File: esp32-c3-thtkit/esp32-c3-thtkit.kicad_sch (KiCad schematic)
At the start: 27 parts, among them J1 PIN_GROUP_1, J2 PIN_GROUP_3, J3 PIN_GROUP_2, J4 UART, U1 MIC5219-3.3YM5, U2 ESP32-C3, Y1 32.768kHz ±20ppm CL12.5pF, Y2 40MHz ±10ppm CL8pF

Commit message: Change some manufacturing related attributes
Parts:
- J1, J2, TP1, TP2: now left out of the parts list
- U2: LCSC PN (none) -> C2858491
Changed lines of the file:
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@@
 		(unit 1)
 		(exclude_from_sim no)
-		(in_bom yes)
+		(in_bom no)
 		(on_board yes)
 		(dnp no)
@@
 		(unit 1)
 		(exclude_from_sim no)
-		(in_bom yes)
+		(in_bom no)
 		(on_board yes)
 		(dnp no)
@@
 		(unit 1)
 		(exclude_from_sim no)
-		(in_bom yes)
+		(in_bom no)
 		(on_board yes)
 		(dnp no)
@@
 		(unit 1)
 		(exclude_from_sim no)
-		(in_bom yes)
+		(in_bom no)
 		(on_board yes)
 		(dnp no)
@@
 			)
 		)
-		(property "LCSC PN" ""
+		(property "LCSC PN" "C2858491"
 			(at 123.19 115.57 0)
 			(effects

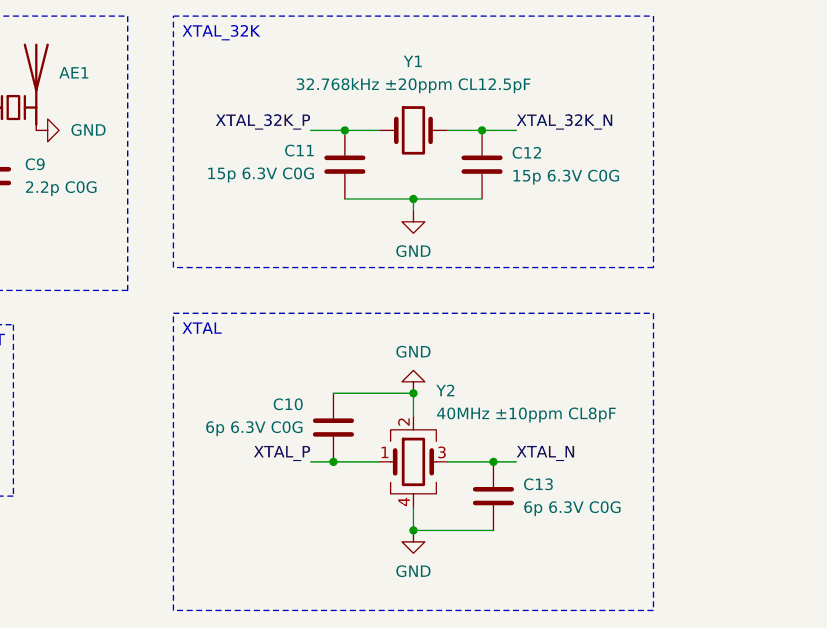
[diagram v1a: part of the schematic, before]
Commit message: Make devkits cheaper by using 0402 components instead of 0201
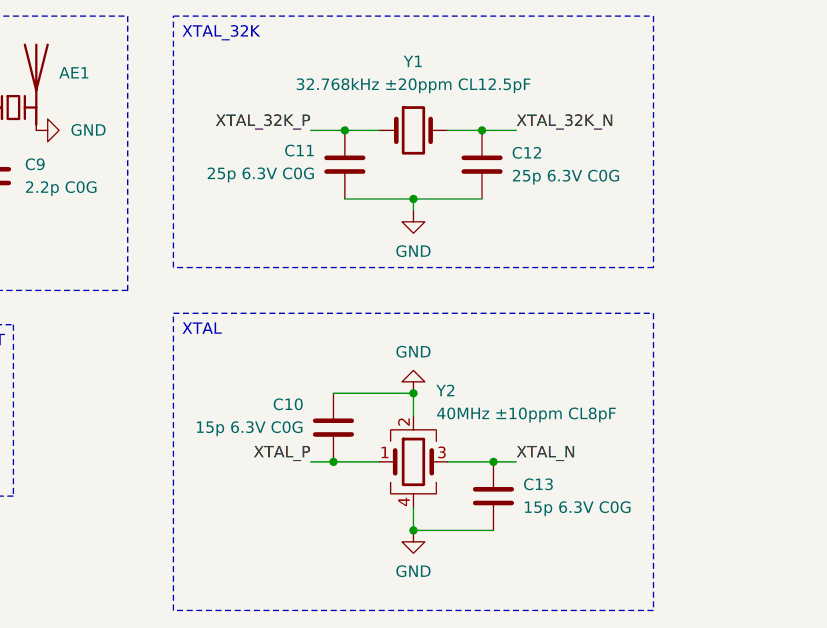
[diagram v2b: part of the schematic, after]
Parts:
- C10: value 6p 6.3V C0G -> 15p 6.3V C0G; footprint Capacitor_SMD:C_0201_0603Metric -> Capacitor_SMD:C_0402_1005Metric; LCSC PN C161434 -> C1548
- C11: value 15p 6.3V C0G -> 25p 6.3V C0G; footprint Capacitor_SMD:C_0201_0603Metric -> Capacitor_SMD:C_0402_1005Metric; LCSC PN C22374851 -> C1556
- C12: value 15p 6.3V C0G -> 25p 6.3V C0G; footprint Capacitor_SMD:C_0201_0603Metric -> Capacitor_SMD:C_0402_1005Metric; LCSC PN C237455 -> C1556
- C13: value 6p 6.3V C0G -> 15p 6.3V C0G; footprint Capacitor_SMD:C_0201_0603Metric -> Capacitor_SMD:C_0402_1005Metric; LCSC PN C237455 -> C1548
- C2: footprint Capacitor_SMD:C_0201_0603Metric -> Capacitor_SMD:C_0402_1005Metric; LCSC PN C694489 -> C1537
- C7: footprint Capacitor_SMD:C_0201_0603Metric -> Capacitor_SMD:C_0402_1005Metric; LCSC PN C85914 -> C1574
- C9: footprint Capacitor_SMD:C_0201_0603Metric -> Capacitor_SMD:C_0402_1005Metric; LCSC PN C710732 -> C1559
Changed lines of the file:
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@@
 		(title "ESP32-C3-THTKIT")
 		(date "2025-05-31")
-		(rev "1.0.0")
+		(rev "1.0.1")
 		(company "SIVAKOV.TECH")
 	)
@@
 			)
 		)
-		(property "Value" "6p 6.3V C0G"
+		(property "Value" "15p 6.3V C0G"
 			(at 212.598 132.08 0)
 			(effects
@@
 			)
 		)
-		(property "Footprint" "Capacitor_SMD:C_0201_0603Metric"
+		(property "Footprint" "Capacitor_SMD:C_0402_1005Metric"
 			(at 214.9348 128.27 0)
 			(effects
@@
 			)
 		)
-		(property "LCSC PN" "C161434"
+		(property "LCSC PN" "C1548"
 			(at 215.9 132.08 0)
 			(effects
@@
 			)
 		)
-		(property "Footprint" "Capacitor_SMD:C_0201_0603Metric"
+		(property "Footprint" "Capacitor_SMD:C_0402_1005Metric"
 			(at 176.8348 100.33 0)
 			(effects
@@
 			)
 		)
-		(property "LCSC PN" "C710732"
+		(property "LCSC PN" "C1559"
 			(at 177.8 104.14 0)
 			(effects
@@
 			)
 		)
-		(property "Footprint" "Capacitor_SMD:C_0201_0603Metric"
+		(property "Footprint" "Capacitor_SMD:C_0402_1005Metric"
 			(at 79.0448 58.42 0)
 			(effects
@@
 			)
 		)
-		(property "LCSC PN" "C694489"
+		(property "LCSC PN" "C1537"
 			(at 80.01 62.23 0)
 			(effects
@@
 			)
 		)
-		(property "Footprint" "Capacitor_SMD:C_0201_0603Metric"
+		(property "Footprint" "Capacitor_SMD:C_0402_1005Metric"
 			(at 167.64 100.0252 0)
 			(effects
@@
 			)
 		)
-		(property "LCSC PN" "C85914"
+		(property "LCSC PN" "C1574"
 			(at 171.45 99.06 90)
 			(effects
@@
 			)
 		)
-		(property "Value" "6p 6.3V C0G"
+		(property "Value" "15p 6.3V C0G"
 			(at 236.982 140.97 0)
 			(effects
@@
 			)
 		)
-		(property "Footprint" "Capacitor_SMD:C_0201_0603Metric"
+		(property "Footprint" "Capacitor_SMD:C_0402_1005Metric"
 			(at 232.7148 135.89 0)
 			(effects
@@
 			)
 		)
-		(property "LCSC PN" "C237455"
+		(property "LCSC PN" "C1548"
 			(at 233.68 139.7 0)
 			(effects
@@
 			)
 		)
-		(property "Value" "15p 6.3V C0G"
+		(property "Value" "25p 6.3V C0G"
 			(at 213.868 103.886 0)
 			(effects
@@
 			)
 		)
-		(property "Footprint" "Capacitor_SMD:C_0201_0603Metric"
+		(property "Footprint" "Capacitor_SMD:C_0402_1005Metric"
 			(at 216.2048 99.06 0)
 			(effects
@@
 			)
 		)
-		(property "LCSC PN" "C22374851"
+		(property "LCSC PN" "C1556"
 			(at 217.17 102.87 0)
 			(effects
@@
 			)
 		)
-		(property "Value" "15p 6.3V C0G"
+		(property "Value" "25p 6.3V C0G"
 			(at 235.712 104.14 0)
 			(effects
@@
 			)
 		)
-		(property "Footprint" "Capacitor_SMD:C_0201_0603Metric"
+		(property "Footprint" "Capacitor_SMD:C_0402_1005Metric"
 			(at 231.4448 99.06 0)
 			(effects
@@
 			)
 		)
-		(property "LCSC PN" "C237455"
+		(property "LCSC PN" "C1556"
 			(at 232.41 102.87 0)
 			(effects

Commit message: Change microcontroller package from 4x4 to 5x5
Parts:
- U2: footprint PCM_SKC_MCU_Espressif:TQFN_32_1EP_4x4mm_P0.4mm_EP2.4x2.4mm_Compact -> PCM_SKC_MCU_Espressif:VFQFN_32_1EP_5x5mm_P0.5mm_EP3.2x3.2mm_Compact
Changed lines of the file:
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@@
 			)
 		)
-		(property "Footprint" "PCM_SKC_MCU_Espressif:TQFN_32_1EP_4x4mm_P0.4mm_EP2.4x2.4mm_Compact"
+		(property "Footprint" "PCM_SKC_MCU_Espressif:VFQFN_32_1EP_5x5mm_P0.5mm_EP3.2x3.2mm_Compact"
 			(at 97.79 85.09 0)
 			(effects

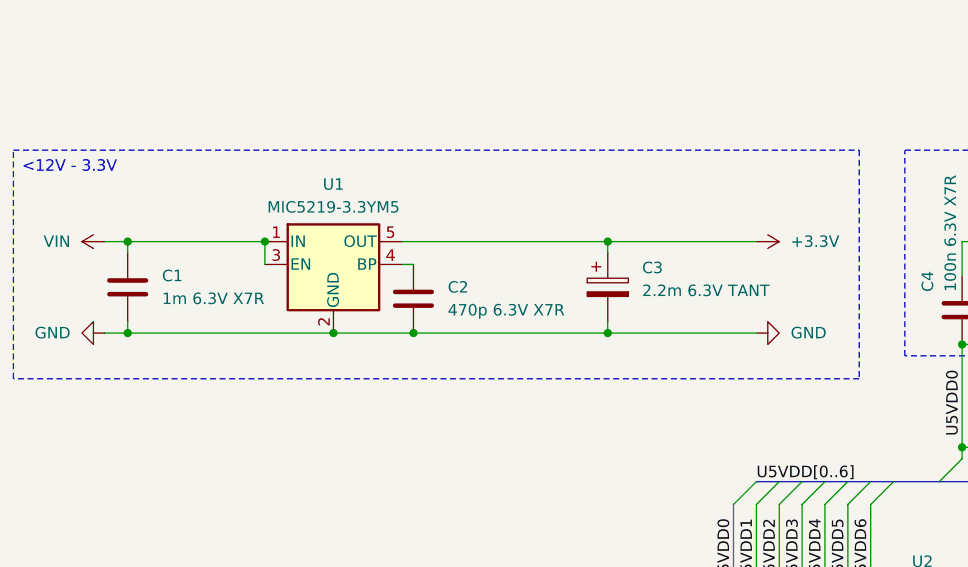
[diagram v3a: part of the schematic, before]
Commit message: Unify schemas and fix esp32-c3 footprint
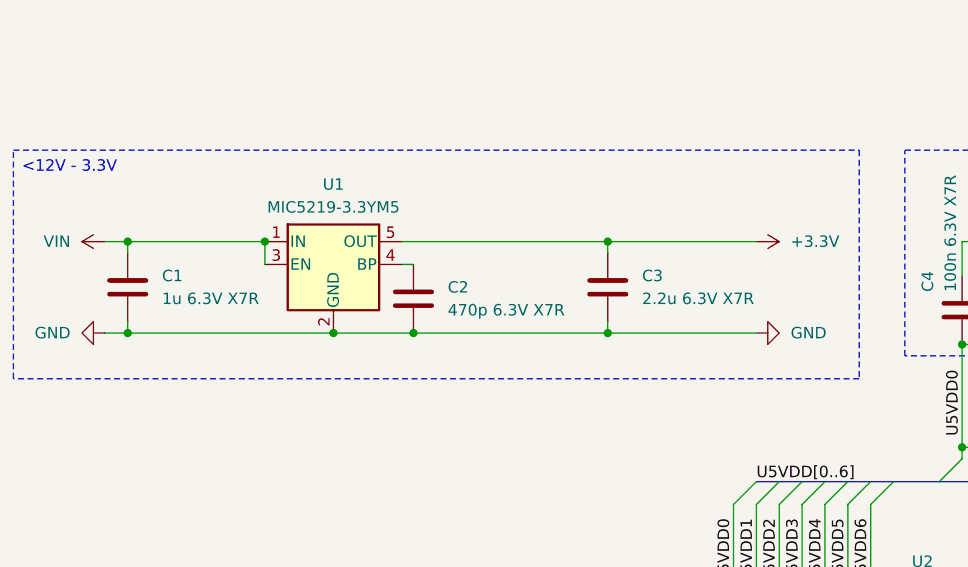
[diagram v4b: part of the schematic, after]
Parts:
- removed C3: 2.2m 6.3V TANT, Capacitor_Tantalum_SMD:CP_EIA-2012-12_Kemet-R, symbol Device:C_Polarized
- added C3: 2.2u 6.3V X7R, Capacitor_SMD:C_0402_1005Metric, symbol Device:C
- C1: value 1m 6.3V X7R -> 1u 6.3V X7R; Mouser PN DRAFT (none) -> 963-TMK105BJ105MV-F
- C10, C13: Mouser PN DRAFT (none) -> 963-MCASU105SCG150JF
- C11, C12: Mouser PN DRAFT (none) -> 603-CC0402JRNPO9BN25
- C2: Mouser PN DRAFT (none) -> 963-MCASU105SB7471KF
- C4, C5, C6, C8: Mouser PN DRAFT (none) -> 963-MLASU105SB7104KF
- C7: Mouser PN DRAFT (none) -> 963-MCASU105SCG5R6CF
- C9: Mouser PN DRAFT (none) -> 963-MBASU105SCG2R2BF
- L1: Mouser PN DRAFT (none) -> 81-LQG15HS3N9B02D
- R1, R2: Mouser PN DRAFT (none) -> 667-ERJ-PA2D1002X
- U1: Mouser PN DRAFT (none) -> 998-MIC5219-3.3YM5TR
- U2: Mouser PN DRAFT (none) -> 356-ESP32-C3FH4
- Y1: Mouser PN DRAFT (none) -> 815-ABS05N32768KH9T5
- Y2: Mouser PN DRAFT (none) -> 815-11W40-8B1UT
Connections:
- net +3.3V: now also C3.2
- net GND: now also C3.1
